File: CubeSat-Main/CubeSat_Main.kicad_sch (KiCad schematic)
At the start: 20 parts, among them J1 Conn_01x03_Pin, J2 Conn_01x08_Socket, U1 STM32F411CEU6 - BlackPill, U2 LORA E220-900T22D, U3 BNO055, U4 GPS_NEO6M, U6 LM35-LP

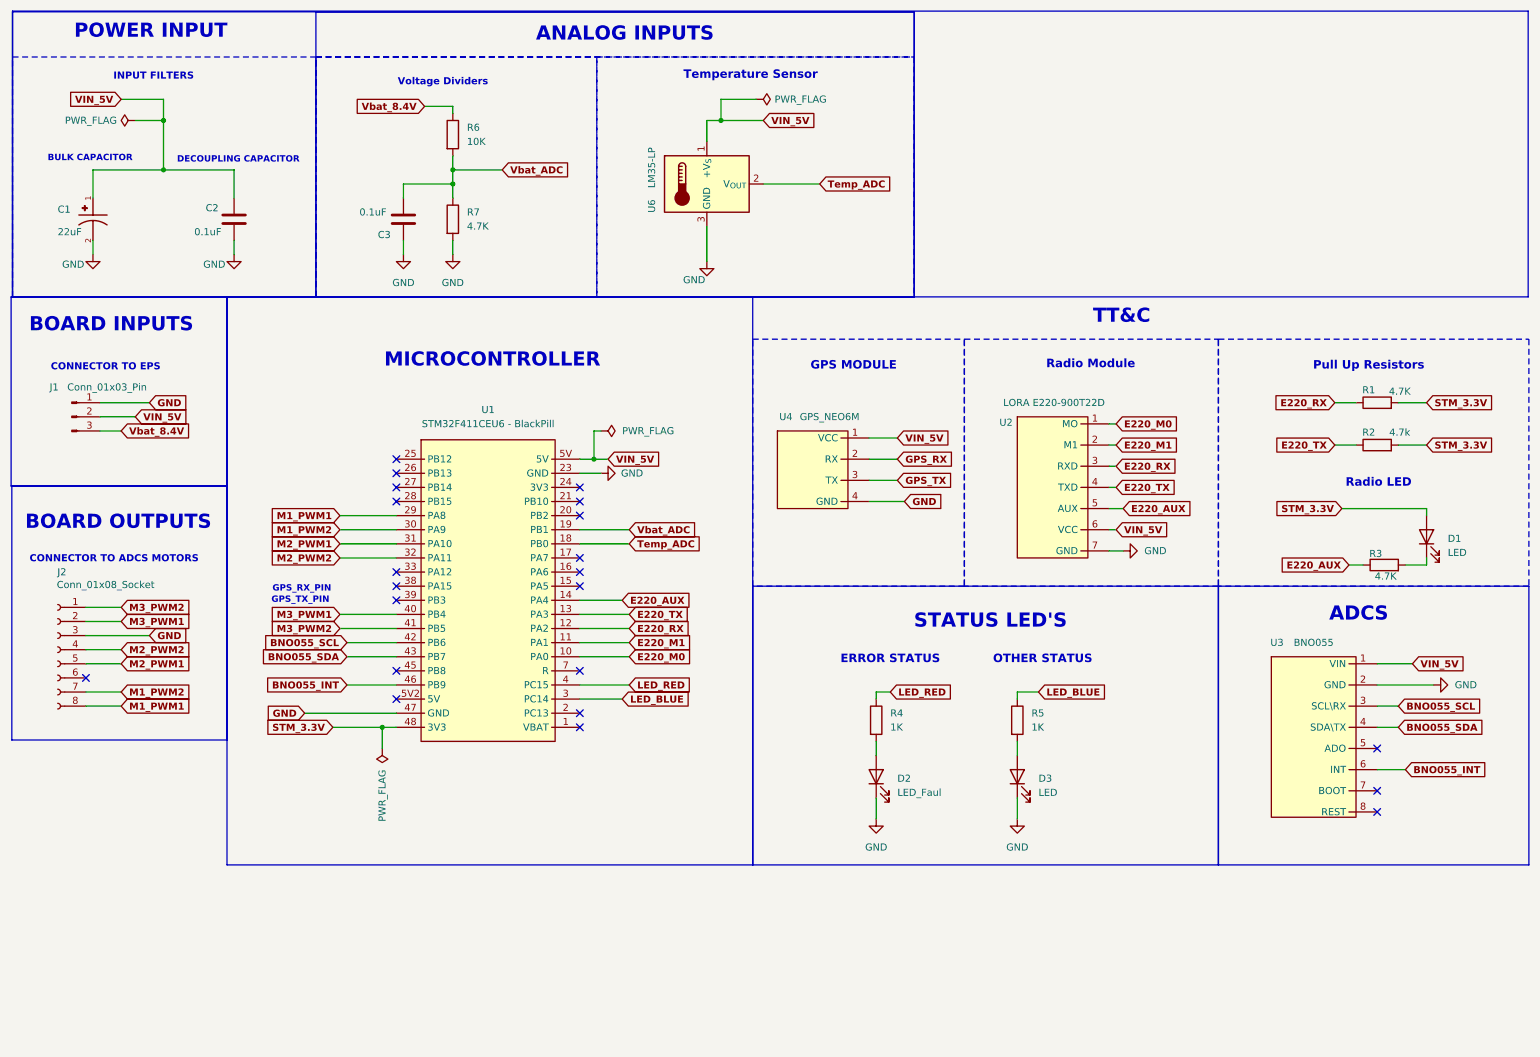
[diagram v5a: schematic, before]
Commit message: new Main and EPS PCBs, all previous problems corrected, final version
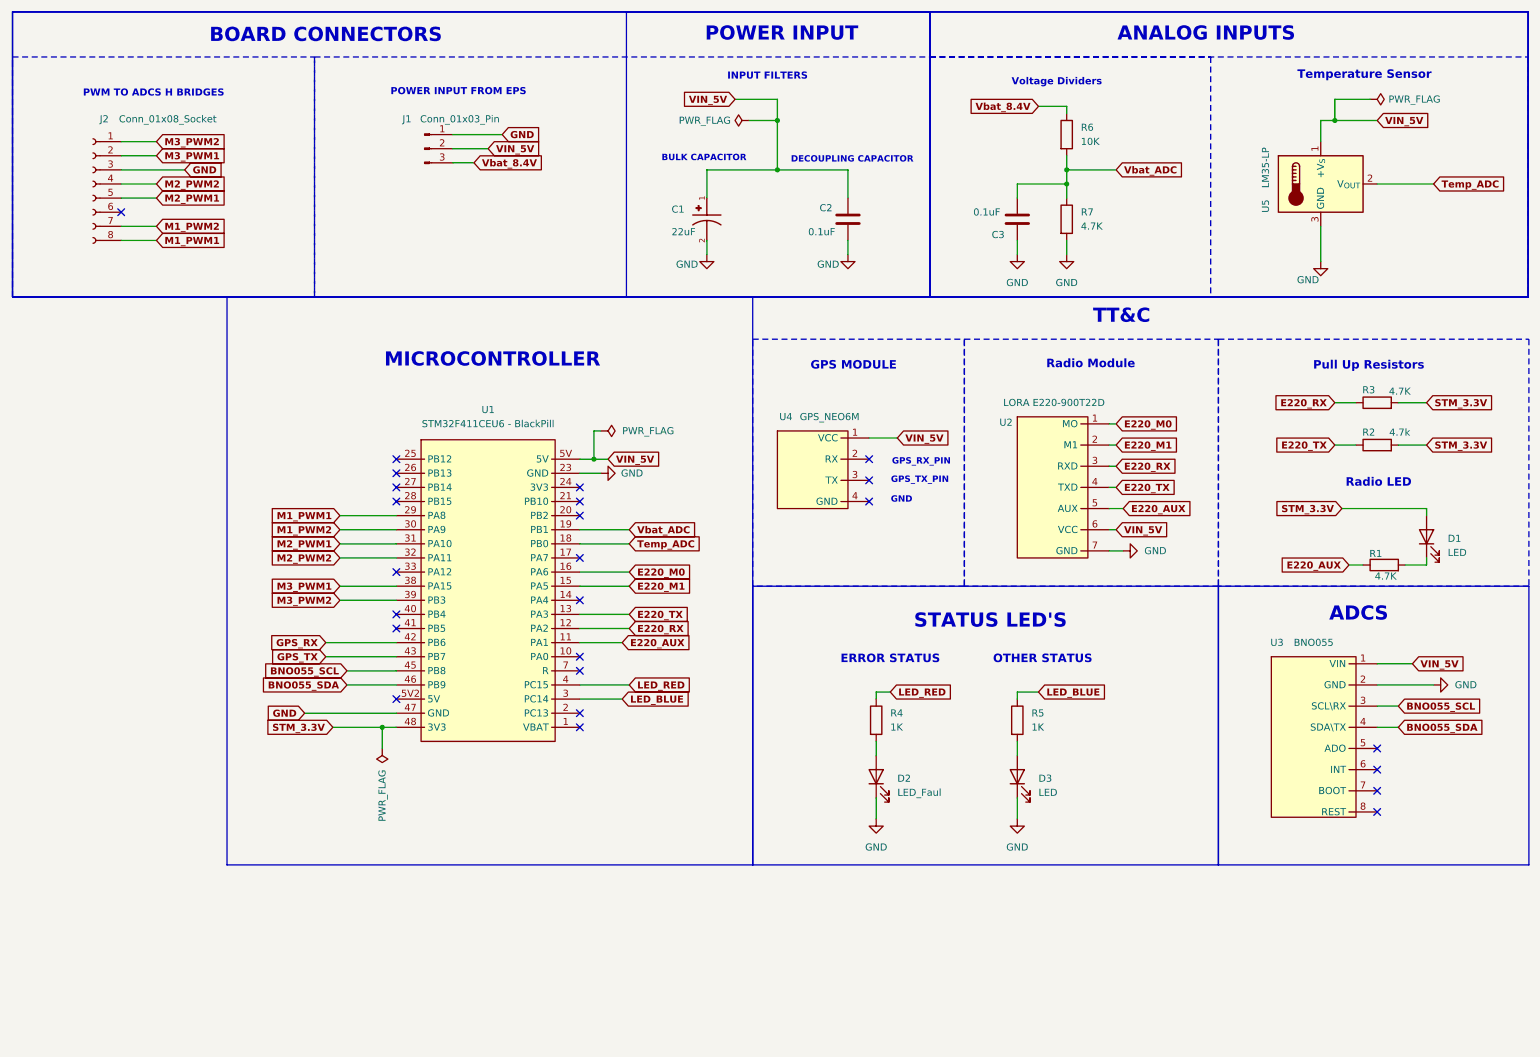
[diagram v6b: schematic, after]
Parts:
- renumbered R3 to R1, R1 to R3, U6 to U5
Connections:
- net BNO055_SCL: now also U1.45 (PB8); no longer U1.42 (PB6)
- net BNO055_SDA: now also U1.46 (PB9); no longer U1.43 (PB7)
- net E220_AUX: now also U1.11 (PA1); no longer U1.14 (PA4)
- net E220_M0: now also U1.16 (PA6); no longer U1.10 (PA0)
- net E220_M1: now also U1.15 (PA5); no longer U1.11 (PA1)
- net GND: no longer U4.4 (GND)
- net GPS_RX: now also U1.42 (PB6); no longer U4.2 (RX)
- net GPS_TX: now also U1.43 (PB7); no longer U4.3 (TX)
- net M3_PWM1: now also U1.38 (PA15); no longer U1.40 (PB4)
- net M3_PWM2: now also U1.39 (PB3); no longer U1.41 (PB5)
- net BNO055_INT: no longer names the net of U3.6 (INT)
- net BNO055_INT: no longer U1.46 (PB9)
- no-connect marks 22 -> 25
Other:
- note added: "BOARD CONNECTORS"
- note added: "GND"
- note added: "POWER INPUT FROM EPS"
- note added: "PWM TO ADCS H BRIDGES"
- note removed: "BOARD INPUTS"
- note removed: "BOARD OUTPUTS"
- note removed: "CONNECTOR TO ADCS MOTORS"
- note removed: "CONNECTOR TO EPS"
- moved on the sheet: C1, C2, C3, J1, J2, R6, R7, U5

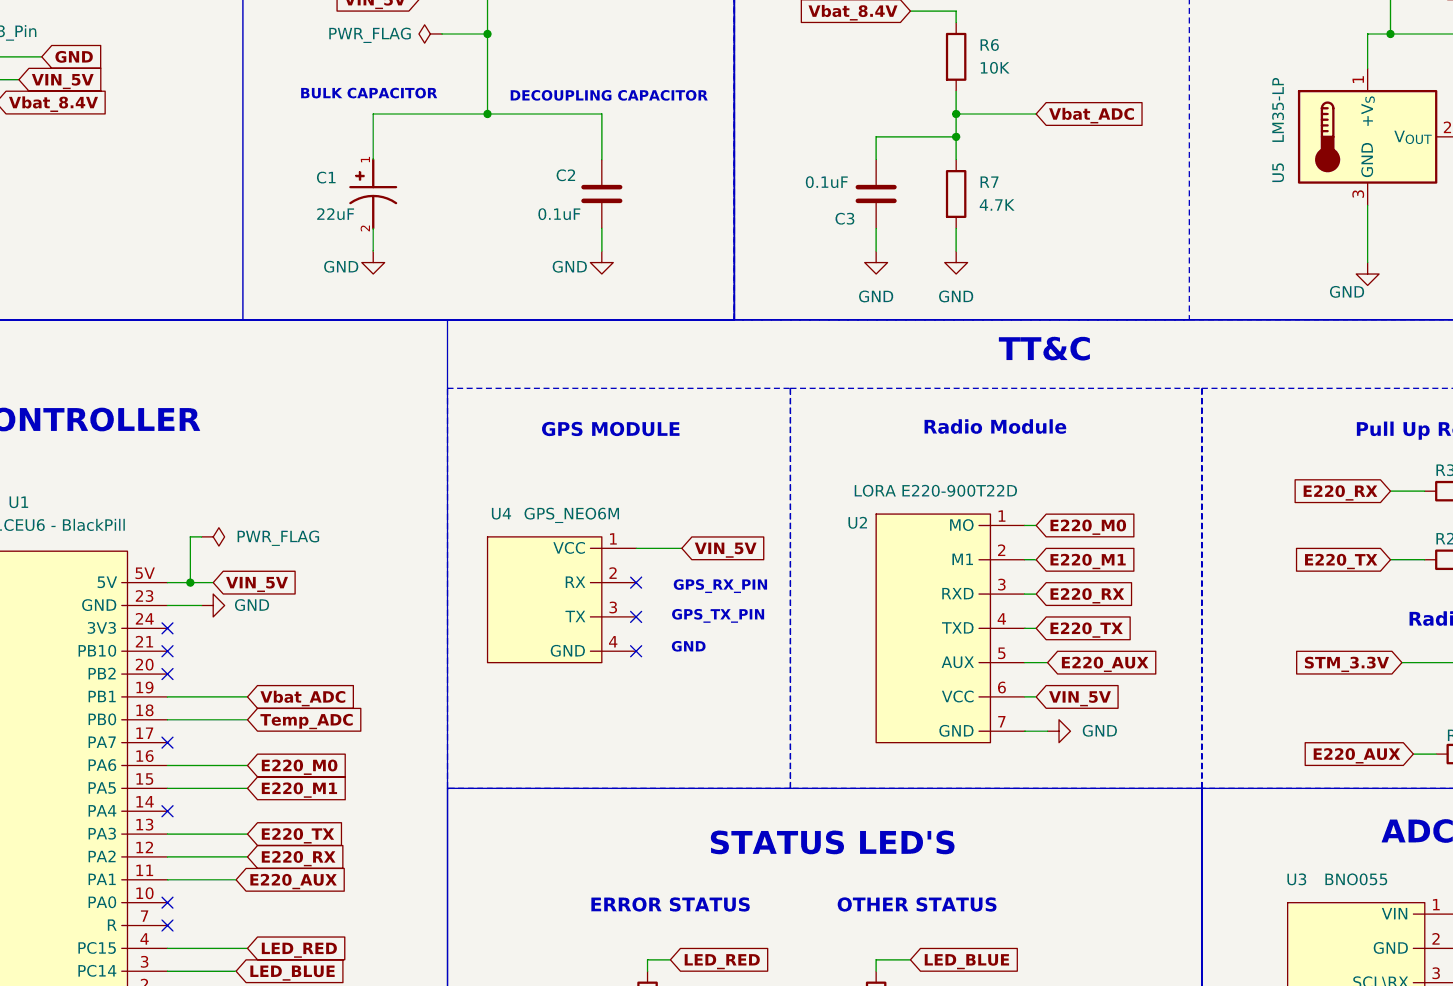
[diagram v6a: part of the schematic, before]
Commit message: adding the unused pin as smd, instead of just removing it
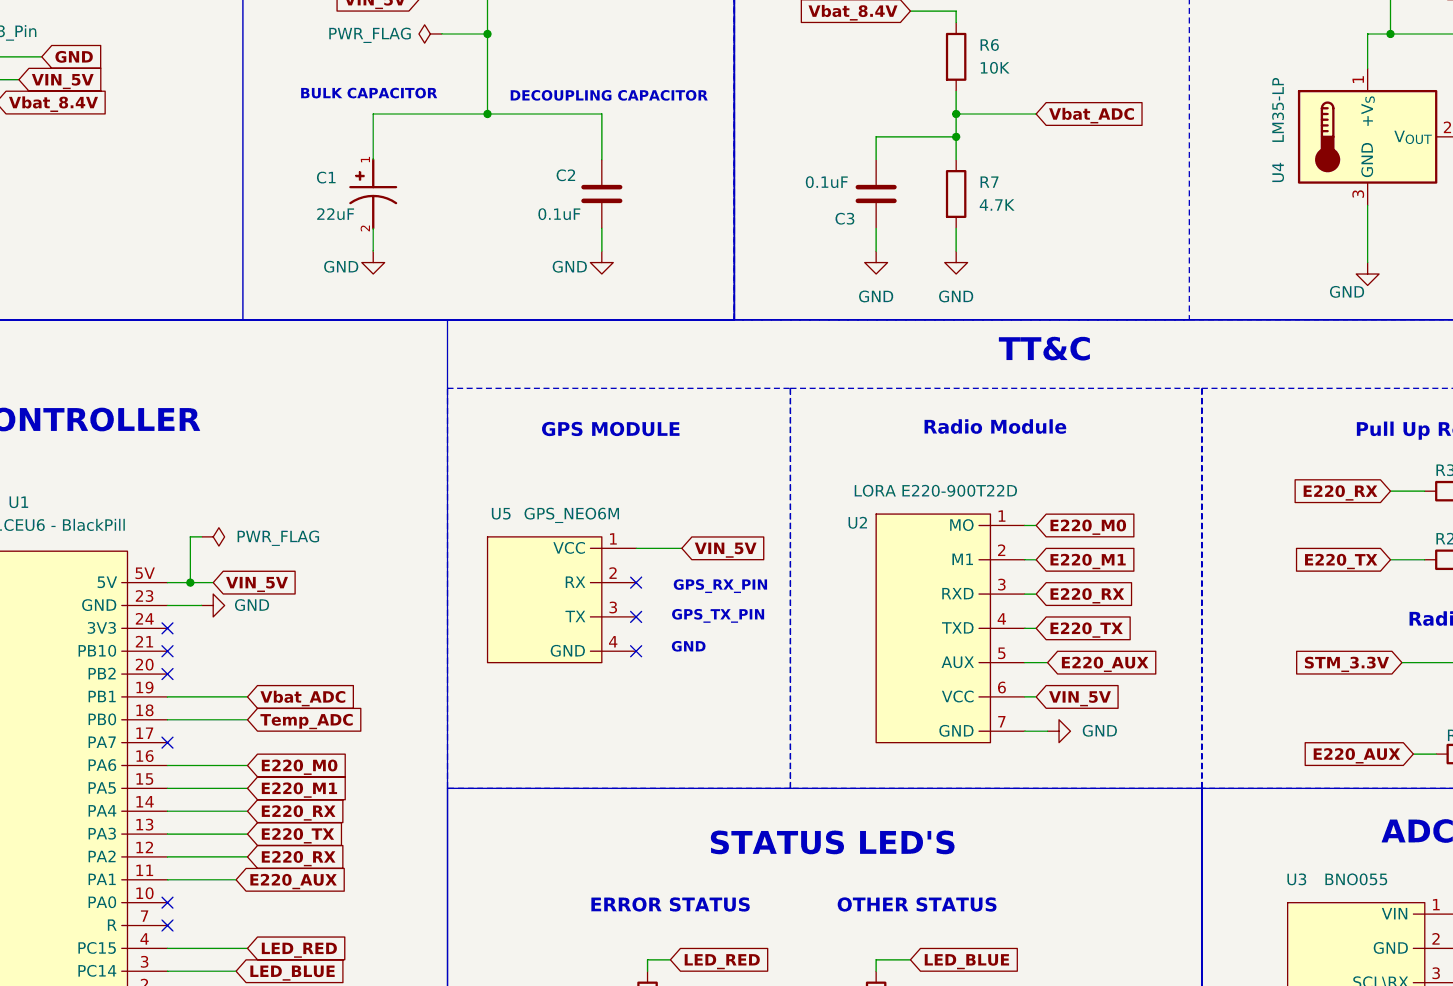
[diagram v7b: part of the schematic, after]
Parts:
- renumbered U5 to U4, U4 to U5
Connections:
- net E220_RX: now also U1.14 (PA4)
- no-connect marks 25 -> 24
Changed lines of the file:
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@@
 	)
 	(no_connect
-		(at 114.3 118.11)
-	)
-	(no_connect
 		(at 114.3 140.97)
 	)
@@
 	(wire
 		(pts
+			(xy 114.3 118.11) (xy 123.19 118.11)
+		)
+		(stroke
+			(width 0)
+			(type default)
+		)
+	)
+	(wire
+		(pts
 			(xy 257.81 129.54) (xy 264.16 129.54)
 		)
@@
 		)
 	)
+	(global_label "E220_RX"
+		(shape input)
+		(at 123.19 118.11 0)
+		(fields_autoplaced yes)
+		(effects
+			(font
+				(size 1.27 1.27)
+				(thickness 0.254)
+				(bold yes)
+			)
+			(justify left)
+		)
+		(property "Intersheetrefs" "${INTERSHEET_REFS}"
+			(at 134.8758 118.11 0)
+			(effects
+				(font
+					(size 1.27 1.27)
+				)
+				(justify left)
+				(hide yes)
+			)
+		)
+	)
 	(global_label "Vbat_8.4V"
 		(shape input)
@@
 		(on_board yes)
 		(dnp no)
-		(property "Reference" "U5"
+		(property "Reference" "U4"
 			(at 237.744 45.974 90)
 			(effects
@@
 			(project ""
 				(path "/efe2bccd-e118-4ad0-853a-c0e965c7d995"
-					(reference "U5")
+					(reference "U4")
 					(unit 1)
 				)
@@
 		(on_board yes)
 		(dnp no)
-		(property "Reference" "U4"
+		(property "Reference" "U5"
 			(at 151.384 85.09 0)
 			(effects
@@
 			(project ""
 				(path "/efe2bccd-e118-4ad0-853a-c0e965c7d995"
-					(reference "U4")
+					(reference "U5")
 					(unit 1)
 				)

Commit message: small changes in layout
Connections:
- net M1_PWM1: now also U1.26 (PB13); no longer U1.29 (PA8)
- net M1_PWM2: now also U1.27 (PB14); no longer U1.30 (PA9)
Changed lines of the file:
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@@
+	)
+	(no_connect
+		(at 81.28 102.87)
 	)
 	(no_connect
@@
 	)
 	(no_connect
+		(at 81.28 105.41)
+	)
+	(no_connect
 		(at 257.81 144.78)
 	)
@@
 	)
 	(no_connect
-		(at 81.28 95.25)
-	)
-	(no_connect
-		(at 81.28 97.79)
-	)
-	(no_connect
 		(at 114.3 138.43)
 	)
@@
 	(wire
 		(pts
+			(xy 71.12 97.79) (xy 81.28 97.79)
+		)
+		(stroke
+			(width 0)
+			(type default)
+		)
+	)
+	(wire
+		(pts
 			(xy 71.12 107.95) (xy 81.28 107.95)
 		)
@@
 	(wire
 		(pts
-			(xy 71.12 105.41) (xy 81.28 105.41)
-		)
-		(stroke
-			(width 0)
-			(type default)
-		)
-	)
-	(wire
-		(pts
 			(xy 209.55 93.98) (xy 210.82 93.98)
 		)
@@
 	(wire
 		(pts
-			(xy 71.12 102.87) (xy 81.28 102.87)
-		)
-		(stroke
-			(width 0)
-			(type default)
-		)
-	)
-	(wire
-		(pts
 			(xy 68.58 125.73) (xy 81.28 125.73)
 		)
@@
 	(wire
 		(pts
+			(xy 71.12 95.25) (xy 81.28 95.25)
+		)
+		(stroke
+			(width 0)
+			(type default)
+		)
+	)
+	(wire
+		(pts
 			(xy 31.75 38.1) (xy 38.1 38.1)
 		)
@@
 	(global_label "M1_PWM1"
 		(shape input)
-		(at 71.12 102.87 180)
+		(at 71.12 95.25 180)
 		(fields_autoplaced yes)
 		(effects
@@
 		)
 		(property "Intersheetrefs" "${INTERSHEET_REFS}"
-			(at 58.648 102.87 0)
+			(at 58.648 95.25 0)
 			(effects
 				(font
@@
 	(global_label "M1_PWM2"
 		(shape input)
-		(at 71.12 105.41 180)
+		(at 71.12 97.79 180)
 		(fields_autoplaced yes)
 		(effects
@@
 		)
 		(property "Intersheetrefs" "${INTERSHEET_REFS}"
-			(at 58.648 105.41 0)
-			(effects
-				(font
+			(at 58.648 97.79 0)
+			(effects
+				(font
